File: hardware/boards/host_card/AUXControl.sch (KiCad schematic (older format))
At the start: 1 part, among them U1 ECP5UM5G-381caBGA

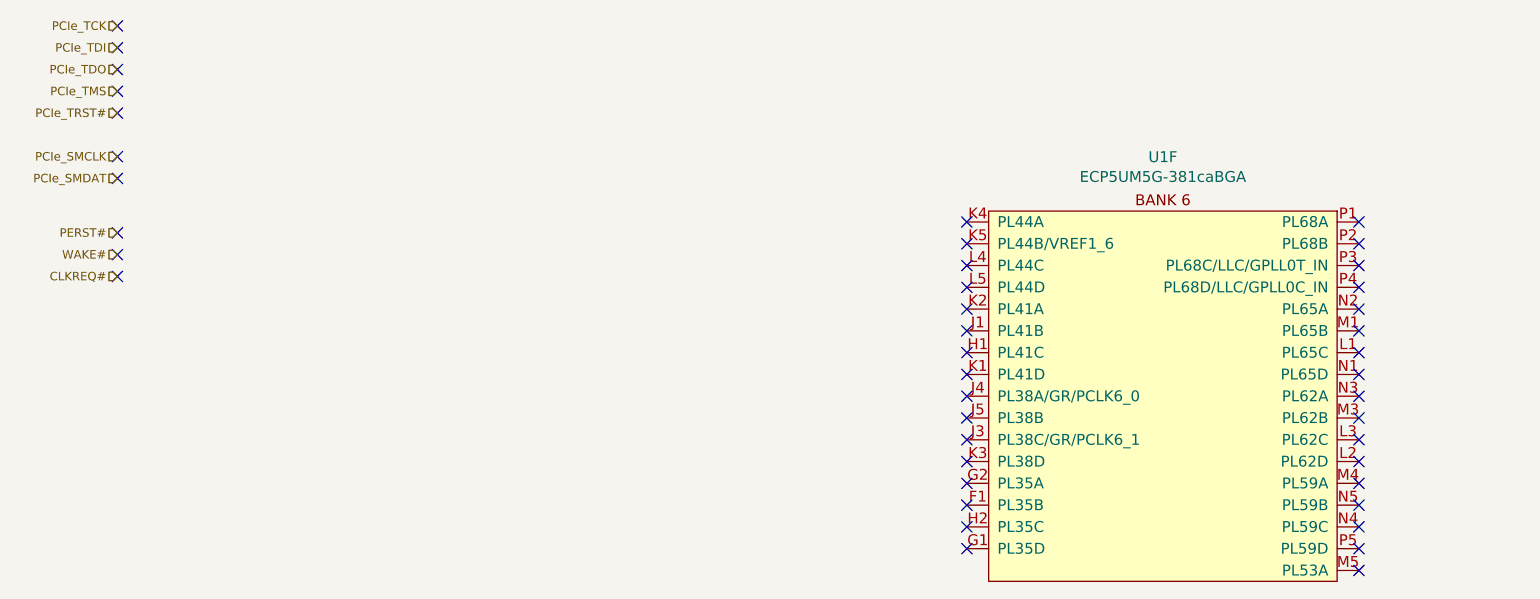
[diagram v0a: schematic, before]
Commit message: Hooked up the PCIe SMBUS and JTAG lines to the FPGA, might need to shuffle the signals around a little bit to get it to route nicely
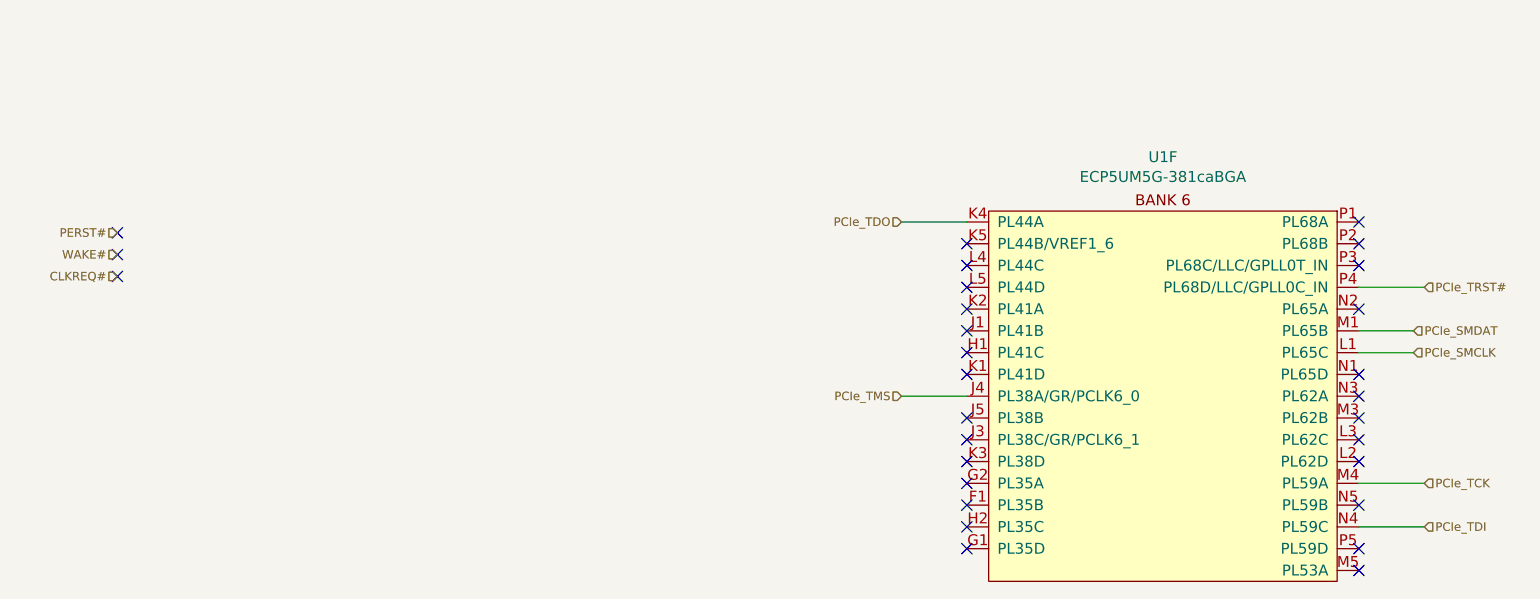
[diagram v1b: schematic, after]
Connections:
- net PCIe_SMCLK: now also U1.L1 (PL65C)
- net PCIe_SMDAT: now also U1.M1 (PL65B)
- net PCIe_TCK: now also U1.M4 (PL59A)
- net PCIe_TDI: now also U1.N4 (PL59C)
- net PCIe_TDO: now also U1.K4 (PL44A)
- net PCIe_TMS: now also U1.J4 (PL38A/GR/PCLK6_0)
- net PCIe_TRST#: now also U1.P4 (PL68D/LLC/GPLL0C_IN)
- no-connect marks 43 -> 29
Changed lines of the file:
@@
 Comment4 ""
 $EndDescr
-Text HLabel 1100 750  0    39   Input ~ 0
+Text HLabel 7100 2850 2    39   Input ~ 0
 PCIe_TCK
-Text HLabel 1100 850  0    39   Input ~ 0
+Text HLabel 7100 3050 2    39   Input ~ 0
 PCIe_TDI
-Text HLabel 1100 950  0    39   Input ~ 0
+Text HLabel 4700 1650 0    39   Input ~ 0
 PCIe_TDO
-Text HLabel 1100 1050 0    39   Input ~ 0
+Text HLabel 4700 2450 0    39   Input ~ 0
 PCIe_TMS
-Text HLabel 1100 1150 0    39   Input ~ 0
+Text HLabel 7100 1950 2    39   Input ~ 0
 PCIe_TRST#
-Text HLabel 1100 1350 0    39   Input ~ 0
+Text HLabel 7050 2250 2    39   Input ~ 0
 PCIe_SMCLK
-Text HLabel 1100 1450 0    39   Input ~ 0
+Text HLabel 7050 2150 2    39   Input ~ 0
 PCIe_SMDAT
 Text HLabel 1100 1700 0    39   Input ~ 0
@@
 Text HLabel 1100 1900 0    39   Input ~ 0
 CLKREQ#
-NoConn ~ 5000 1650
 NoConn ~ 5000 1750
 NoConn ~ 5000 1850
@@
 NoConn ~ 5000 2250
 NoConn ~ 5000 2350
-NoConn ~ 5000 2450
-NoConn ~ 5000 2550
 NoConn ~ 5000 2650
 NoConn ~ 5000 2750
@@
 NoConn ~ 6800 1750
 NoConn ~ 6800 1850
-NoConn ~ 6800 1950
 NoConn ~ 6800 2050
-NoConn ~ 6800 2150
-NoConn ~ 6800 2250
 NoConn ~ 6800 2350
 NoConn ~ 6800 2450
 NoConn ~ 6800 2550
 NoConn ~ 6800 2650
-NoConn ~ 1100 750
-NoConn ~ 1100 850
-NoConn ~ 1100 950
-NoConn ~ 1100 1050
-NoConn ~ 1100 1150
-NoConn ~ 1100 1350
-NoConn ~ 1100 1450
 NoConn ~ 1100 1700
 NoConn ~ 1100 1800
 NoConn ~ 1100 1900
+NoConn ~ 5000 3050
+NoConn ~ 5000 3150
+NoConn ~ 6800 2750
+NoConn ~ 6800 2950
+NoConn ~ 6800 3150
+NoConn ~ 6800 3250
+Wire Wire Line
+	6800 2250 7050 2250
+Wire Wire Line
+	6800 2150 7050 2150
 $Comp
 L lethalbit:ECP5UM5G-381caBGA U?
@@
 	-1   0    0    -1
 $EndComp
-NoConn ~ 5000 3050
-NoConn ~ 5000 3150
-NoConn ~ 6800 2750
-NoConn ~ 6800 2850
-NoConn ~ 6800 2950
-NoConn ~ 6800 3050
-NoConn ~ 6800 3150
-NoConn ~ 6800 3250
+NoConn ~ 5000 2550
+Wire Wire Line
+	6800 3050 7100 3050
+Wire Wire Line
+	6800 2850 7100 2850
+Wire Wire Line
+	6800 1950 7100 1950
+Wire Wire Line
+	4700 2450 5000 2450
+Wire Wire Line
+	4700 1650 5000 1650
 $EndSCHEMATC

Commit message: Added the remainder of the PCIe aux signals to the FPGA
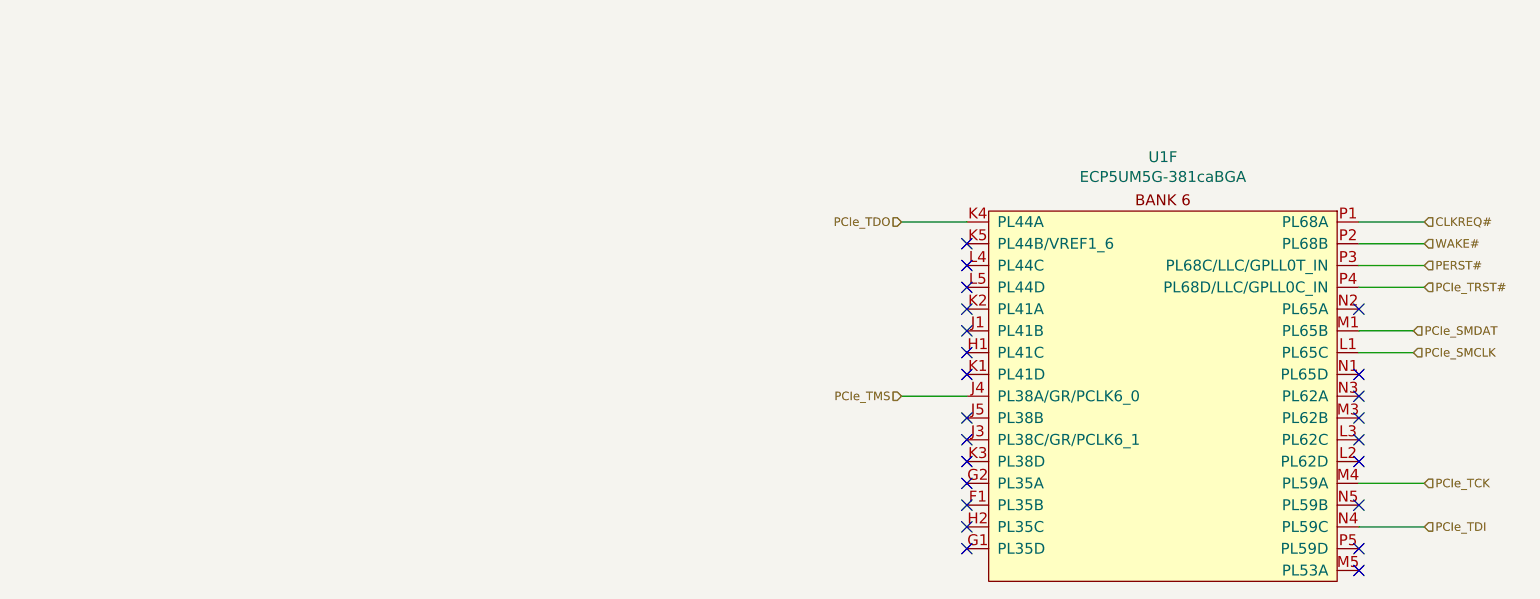
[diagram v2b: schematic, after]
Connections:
- net CLKREQ#: now also U1.P1 (PL68A)
- net PERST#: now also U1.P3 (PL68C/LLC/GPLL0T_IN)
- net WAKE#: now also U1.P2 (PL68B)
- no-connect marks 29 -> 23
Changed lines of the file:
@@
 Text HLabel 7050 2150 2    39   Input ~ 0
 PCIe_SMDAT
-Text HLabel 1100 1700 0    39   Input ~ 0
+Text HLabel 7100 1850 2    39   Input ~ 0
 PERST#
-Text HLabel 1100 1800 0    39   Input ~ 0
+Text HLabel 7100 1750 2    39   Input ~ 0
 WAKE#
-Text HLabel 1100 1900 0    39   Input ~ 0
+Text HLabel 7100 1650 2    39   Input ~ 0
 CLKREQ#
 NoConn ~ 5000 1750
@@
 NoConn ~ 5000 2850
 NoConn ~ 5000 2950
-NoConn ~ 6800 1650
-NoConn ~ 6800 1750
-NoConn ~ 6800 1850
 NoConn ~ 6800 2050
 NoConn ~ 6800 2350
@@
 NoConn ~ 6800 2550
 NoConn ~ 6800 2650
-NoConn ~ 1100 1700
-NoConn ~ 1100 1800
-NoConn ~ 1100 1900
 NoConn ~ 5000 3050
 NoConn ~ 5000 3150
@@
 Wire Wire Line
 	4700 1650 5000 1650
+Wire Wire Line
+	6800 1650 7100 1650
+Wire Wire Line
+	6800 1750 7100 1750
+Wire Wire Line
+	6800 1850 7100 1850
 $EndSCHEMATC

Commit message: Fixed  / updated the ECP5 symbol for the ECP5UM5G-85K
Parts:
- U1: symbol lethalbit:ECP5UM5G-381caBGA -> lethalbit:LFE5UM5G-85F-8BG381I
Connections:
- net CLKREQ#: now also U1.G2 (PL47A); no longer U1.P1 (PL68A)
- net PCIe_SMCLK: now also U1.J3 (PL50C); no longer U1.L1 (PL65C)
- net PCIe_SMDAT: now also U1.J5 (PL50B); no longer U1.M1 (PL65B)
- net PCIe_TCK: now also U1.K4 (PL56A); no longer U1.M4 (PL59A)
- net PCIe_TDI: now also U1.L4 (PL56C); no longer U1.N4 (PL59C)
- net PCIe_TDO: now also U1.M4 (PL83A); no longer U1.K4 (PL44A)
- net PCIe_TMS: now also U1.N2 (PL89A); no longer U1.J4 (PL38A/GR/PCLK6_0)
- net PCIe_TRST#: now also U1.G1 (PL47D); no longer U1.P4 (PL68D/LLC/GPLL0C_IN)
- net PERST#: now also U1.H2 (PL47C); no longer U1.P3 (PL68C/LLC/GPLL0T_IN)
- net WAKE#: now also U1.F1 (PL47B); no longer U1.P2 (PL68B)
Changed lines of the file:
@@
 Comment4 ""
 $EndDescr
-Text HLabel 7100 2850 2    39   Input ~ 0
+Text HLabel 6650 2850 2    39   Input ~ 0
 PCIe_TCK
-Text HLabel 7100 3050 2    39   Input ~ 0
+Text HLabel 6650 3050 2    39   Input ~ 0
 PCIe_TDI
-Text HLabel 4700 1650 0    39   Input ~ 0
+Text HLabel 5150 1650 0    39   Input ~ 0
 PCIe_TDO
-Text HLabel 4700 2450 0    39   Input ~ 0
+Text HLabel 5150 2450 0    39   Input ~ 0
 PCIe_TMS
-Text HLabel 7100 1950 2    39   Input ~ 0
+Text HLabel 6650 1950 2    39   Input ~ 0
 PCIe_TRST#
-Text HLabel 7050 2250 2    39   Input ~ 0
+Text HLabel 6600 2250 2    39   Input ~ 0
 PCIe_SMCLK
-Text HLabel 7050 2150 2    39   Input ~ 0
+Text HLabel 6600 2150 2    39   Input ~ 0
 PCIe_SMDAT
-Text HLabel 7100 1850 2    39   Input ~ 0
+Text HLabel 6650 1850 2    39   Input ~ 0
 PERST#
-Text HLabel 7100 1750 2    39   Input ~ 0
+Text HLabel 6650 1750 2    39   Input ~ 0
 WAKE#
-Text HLabel 7100 1650 2    39   Input ~ 0
+Text HLabel 6650 1650 2    39   Input ~ 0
 CLKREQ#
-NoConn ~ 5000 1750
-NoConn ~ 5000 1850
-NoConn ~ 5000 1950
-NoConn ~ 5000 2050
-NoConn ~ 5000 2150
-NoConn ~ 5000 2250
-NoConn ~ 5000 2350
-NoConn ~ 5000 2650
-NoConn ~ 5000 2750
-NoConn ~ 5000 2850
-NoConn ~ 5000 2950
-NoConn ~ 6800 2050
-NoConn ~ 6800 2350
-NoConn ~ 6800 2450
-NoConn ~ 6800 2550
-NoConn ~ 6800 2650
-NoConn ~ 5000 3050
-NoConn ~ 5000 3150
-NoConn ~ 6800 2750
-NoConn ~ 6800 2950
-NoConn ~ 6800 3150
-NoConn ~ 6800 3250
+NoConn ~ 5450 1750
+NoConn ~ 5450 1850
+NoConn ~ 5450 1950
+NoConn ~ 5450 2050
+NoConn ~ 5450 2150
+NoConn ~ 5450 2250
+NoConn ~ 5450 2350
+NoConn ~ 5450 2650
+NoConn ~ 5450 2750
+NoConn ~ 5450 2850
+NoConn ~ 5450 2950
+NoConn ~ 6350 2050
+NoConn ~ 6350 2350
+NoConn ~ 6350 2450
+NoConn ~ 6350 2550
+NoConn ~ 6350 2650
+NoConn ~ 5450 3050
+NoConn ~ 5450 3150
+NoConn ~ 6350 2750
+NoConn ~ 6350 2950
+NoConn ~ 6350 3150
+NoConn ~ 6350 3250
 Wire Wire Line
-	6800 2250 7050 2250
+	6350 2250 6600 2250
 Wire Wire Line
-	6800 2150 7050 2150
+	6350 2150 6600 2150
 $Comp
-L lethalbit:ECP5UM5G-381caBGA U?
+L lethalbit:LFE5UM5G-85F-8BG381I U?
 U 6 1 5FD7443A
 P 5900 1700
@@
 	-1   0    0    -1
 $EndComp
-NoConn ~ 5000 2550
+NoConn ~ 5450 2550
 Wire Wire Line
-	6800 3050 7100 3050
+	6350 3050 6650 3050
 Wire Wire Line
-	6800 2850 7100 2850
+	6350 2850 6650 2850
 Wire Wire Line
-	6800 1950 7100 1950
+	6350 1950 6650 1950
 Wire Wire Line
-	4700 2450 5000 2450
+	5150 2450 5450 2450
 Wire Wire Line
-	4700 1650 5000 1650
+	5150 1650 5450 1650
 Wire Wire Line
-	6800 1650 7100 1650
+	6350 1650 6650 1650
 Wire Wire Line
-	6800 1750 7100 1750
+	6350 1750 6650 1750
 Wire Wire Line
-	6800 1850 7100 1850
+	6350 1850 6650 1850
 $EndSCHEMATC
